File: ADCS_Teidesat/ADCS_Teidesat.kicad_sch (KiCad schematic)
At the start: 27 parts, among them U1 MAX2659ELT+T, U2 L86-M33, U3 LSM6DSV16XTR, U4 LIS2MDLTR, U5 TMS5703137DPGEQQ1, Y1 ATX-H13-F-16.000MHz-G100-T

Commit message: Mejora del enrutado y las conexiones de los componentes, además de la  modificación en la distribución de los planos
Optimización de las conexiones, liberando la capa TOP relazándolas en la capa BOTTON. Modificación de la distribución de los planos. Actualmente: TOP Layer (Plano de conexiones 1), Inner Layer 1 (GND), Inner Layer 2 (3V3) y BOTTON Layer (Plano de conexiones 2)
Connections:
- net +3V3: now also H1.47 (Pin_47), H1.48 (Pin_48), H1.49 (Pin_49), H1.50 (Pin_50), H1.51 (Pin_51), H1.52 (Pin_52), H2.18 (Pin_18), H2.19 (Pin_19), H2.20 (Pin_20)
- no-connect marks 238 -> 229
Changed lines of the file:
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@@
 	)
 	(no_connect
-		(at 355.6 102.87)
-	)
-	(no_connect
 		(at 234.95 185.42)
 	)
@@
 	)
 	(no_connect
-		(at 391.16 64.77)
-	)
-	(no_connect
 		(at 391.16 49.53)
 	)
@@
 	)
 	(no_connect
-		(at 391.16 67.31)
-	)
-	(no_connect
 		(at 355.6 59.69)
 	)
@@
 	)
 	(no_connect
-		(at 342.9 105.41)
-	)
-	(no_connect
 		(at 179.07 114.3)
 	)
@@
 	)
 	(no_connect
-		(at 355.6 105.41)
-	)
-	(no_connect
 		(at 342.9 74.93)
 	)
@@
 	)
 	(no_connect
-		(at 355.6 107.95)
-	)
-	(no_connect
 		(at 283.21 124.46)
 	)
@@
 	)
 	(no_connect
-		(at 342.9 107.95)
-	)
-	(no_connect
 		(at 342.9 49.53)
 	)
@@
 	)
 	(no_connect
-		(at 378.46 67.31)
-	)
-	(no_connect
 		(at 342.9 72.39)
 	)
@@
 	)
 	(no_connect
-		(at 342.9 102.87)
-	)
-	(no_connect
 		(at 189.23 30.48)
 	)
@@
 	(wire
 		(pts
+			(xy 364.49 102.87) (xy 355.6 102.87)
+		)
+		(stroke
+			(width 0)
+			(type default)
+		)
+	)
+	(wire
+		(pts
 			(xy 91.44 156.21) (xy 95.25 156.21)
 		)
@@
 	(wire
 		(pts
+			(xy 334.01 107.95) (xy 342.9 107.95)
+		)
+		(stroke
+			(width 0)
+			(type default)
+		)
+	)
+	(wire
+		(pts
 			(xy 88.9 229.87) (xy 95.25 229.87)
 		)
@@
 	(wire
 		(pts
+			(xy 400.05 64.77) (xy 391.16 64.77)
+		)
+		(stroke
+			(width 0)
+			(type default)
+		)
+	)
+	(wire
+		(pts
 			(xy 85.09 147.32) (xy 95.25 147.32)
 		)
@@
 	(wire
 		(pts
+			(xy 364.49 105.41) (xy 355.6 105.41)
+		)
+		(stroke
+			(width 0)
+			(type default)
+		)
+	)
+	(wire
+		(pts
 			(xy 43.18 227.33) (xy 25.4 227.33)
 		)
@@
 	(wire
 		(pts
+			(xy 369.57 67.31) (xy 378.46 67.31)
+		)
+		(stroke
+			(width 0)
+			(type default)
+		)
+	)
+	(wire
+		(pts
 			(xy 24.13 95.25) (xy 22.86 95.25)
 		)
@@
 	(wire
 		(pts
+			(xy 400.05 67.31) (xy 391.16 67.31)
+		)
+		(stroke
+			(width 0)
+			(type default)
+		)
+	)
+	(wire
+		(pts
 			(xy 50.8 264.16) (xy 50.8 266.7)
 		)
@@
 	(wire
 		(pts
+			(xy 364.49 107.95) (xy 355.6 107.95)
+		)
+		(stroke
+			(width 0)
+			(type default)
+		)
+	)
+	(wire
+		(pts
 			(xy 217.17 224.79) (xy 217.17 237.49)
 		)
@@
 	(wire
 		(pts
+			(xy 334.01 102.87) (xy 342.9 102.87)
+		)
+		(stroke
+			(width 0)
+			(type default)
+		)
+	)
+	(wire
+		(pts
 			(xy 102.87 218.44) (xy 102.87 227.33)
 		)
@@
 	(wire
 		(pts
+			(xy 334.01 105.41) (xy 342.9 105.41)
+		)
+		(stroke
+			(width 0)
+			(type default)
+		)
+	)
+	(wire
+		(pts
 			(xy 205.74 234.95) (xy 205.74 251.46)
 		)
@@
 		)
 	)
+	(label "+3V3"
+		(at 364.49 105.41 180)
+		(effects
+			(font
+				(size 1.27 1.27)
+			)
+			(justify right bottom)
+		)
+	)
 	(label "SPC_MAG."
 		(at 304.8 91.44 180)
@@
 		)
 	)
+	(label "+3V3"
+		(at 400.05 67.31 180)
+		(effects
+			(font
+				(size 1.27 1.27)
+			)
+			(justify right bottom)
+		)
+	)
 	(label "SOMI_IMU"
 		(at 304.8 83.82 180)
@@
 		)
 	)
+	(label "+3V3"
+		(at 334.01 105.41 0)
+		(effects
+			(font
+				(size 1.27 1.27)
+			)
+			(justify left bottom)
+		)
+	)
 	(label "DATA_OUT"
 		(at 78.74 154.94 180)
@@
 		)
 	)
+	(label "+3V3"
+		(at 369.57 67.31 0)
+		(effects
+			(font
+				(size 1.27 1.27)
+			)
+			(justify left bottom)
+		)
+	)
 	(label "CS_MAGNETÓMETRO"
 		(at 157.48 111.76 0)
@@
 		)
 	)
+	(label "+3V3"
+		(at 364.49 102.87 180)
+		(effects
+			(font
+				(size 1.27 1.27)
+			)
+			(justify right bottom)
+		)
+	)
 	(label "INT_MAGNETÓMETRO"
 		(at 215.9 232.41 180)
@@
 		)
 	)
+	(label "+3V3"
+		(at 334.01 102.87 0)
+		(effects
+			(font
+				(size 1.27 1.27)
+			)
+			(justify left bottom)
+		)
+	)
 	(label "INT1"
 		(at 34.29 232.41 0)
@@
 		)
 	)
+	(label "+3V3"
+		(at 400.05 64.77 180)
+		(effects
+			(font
+				(size 1.27 1.27)
+			)
+			(justify right bottom)
+		)
+	)
 	(label "INT1"
 		(at 168.91 78.74 0)
@@
 		)
 	)
+	(label "+3V3"
+		(at 364.49 107.95 180)
+		(effects
+			(font
+				(size 1.27 1.27)
+			)
+			(justify right bottom)
+		)
+	)
 	(label "OUT_ANT"
 		(at 60.96 165.1 180)
@@
 		)
 	)
+	(label "+3V3"
+		(at 334.01 107.95 0)
+		(effects
+			(font
+				(size 1.27 1.27)
+			)
+			(justify left bottom)
+		)
+	)
 	(label "RF"
 		(at 58.42 92.71 180)
@@
 		)
 		(property "Value" "+3V3"
-			(at 214.122 220.98 0)
+			(at 213.868 220.726 0)
 			(effects
 				(font

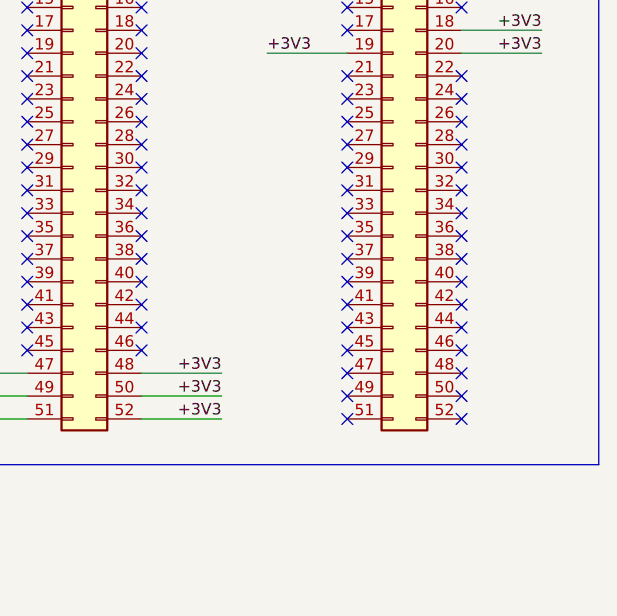
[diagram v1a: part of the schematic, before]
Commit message: Últimas modificaciones de la V.0.1.
Se han realizado las últimas modificaciones en del diseño de la PCB, se han nombrado las capas, y además, se han añadido las huellas correctas de cada componente.
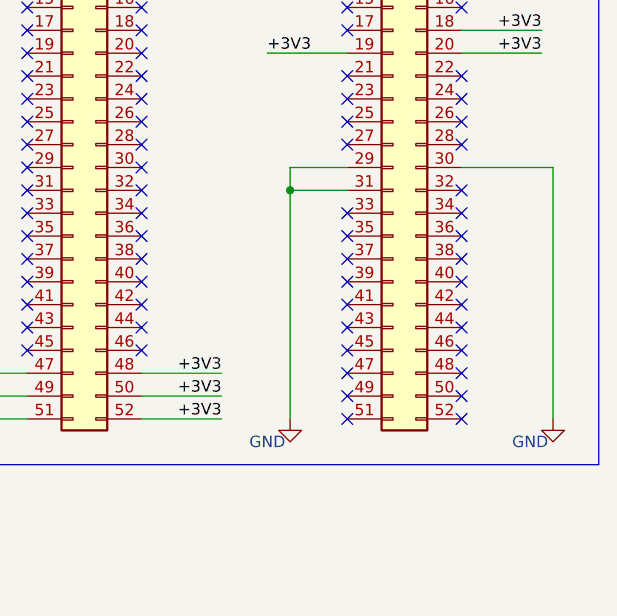
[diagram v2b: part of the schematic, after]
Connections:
- net GND: now also H2.29 (Pin_29), H2.30 (Pin_30), H2.31 (Pin_31)
- no-connect marks 229 -> 226
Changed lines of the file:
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@@
 	)
 	(junction
+		(at 372.11 82.55)
+		(diameter 0)
+		(color 0 0 0 0)
+	)
+	(junction
 		(at 64.77 116.84)
 		(diameter 0)
@@
 	)
 	(no_connect
-		(at 378.46 82.55)
-	)
-	(no_connect
 		(at 234.95 185.42)
 	)
@@
 	)
 	(no_connect
-		(at 391.16 80.01)
-	)
-	(no_connect
 		(at 342.9 44.45)
 	)
@@
 	)
 	(no_connect
-		(at 378.46 80.01)
-	)
-	(no_connect
 		(at 378.46 57.15)
 	)
@@
 	(wire
 		(pts
+			(xy 372.11 82.55) (xy 378.46 82.55)
+		)
+		(stroke
+			(width 0)
+			(type default)
+		)
+	)
+	(wire
+		(pts
 			(xy 66.04 250.19) (xy 66.04 266.7)
 		)
@@
 	(wire
 		(pts
+			(xy 401.32 80.01) (xy 401.32 107.95)
+		)
+		(stroke
+			(width 0)
+			(type default)
+		)
+	)
+	(wire
+		(pts
 			(xy 25.4 72.39) (xy 25.4 73.66)
 		)
@@
 	(wire
 		(pts
+			(xy 391.16 80.01) (xy 401.32 80.01)
+		)
+		(stroke
+			(width 0)
+			(type default)
+		)
+	)
+	(wire
+		(pts
 			(xy 54.61 92.71) (xy 58.42 92.71)
 		)
@@
 	(wire
 		(pts
+			(xy 372.11 107.95) (xy 372.11 82.55)
+		)
+		(stroke
+			(width 0)
+			(type default)
+		)
+	)
+	(wire
+		(pts
 			(xy 369.57 67.31) (xy 378.46 67.31)
 		)
@@
 	(wire
 		(pts
+			(xy 372.11 80.01) (xy 378.46 80.01)
+		)
+		(stroke
+			(width 0)
+			(type default)
+		)
+	)
+	(wire
+		(pts
 			(xy 205.74 251.46) (xy 217.17 251.46)
 		)
@@
 	(wire
 		(pts
+			(xy 372.11 82.55) (xy 372.11 80.01)
+		)
+		(stroke
+			(width 0)
+			(type default)
+		)
+	)
+	(wire
+		(pts
 			(xy 26.67 72.39) (xy 25.4 72.39)
 		)
@@
 	)
 	(symbol
+		(lib_id "power:GND")
+		(at 372.11 107.95 0)
+		(unit 1)
+		(exclude_from_sim no)
+		(in_bom yes)
+		(on_board yes)
+		(dnp no)
+		(property "Reference" "#PWR026"
+			(at 372.11 114.3 0)
+			(effects
+				(font
+					(size 1.27 1.27)
+				)
+				(hide yes)
+			)
+		)
+		(property "Value" "GND"
+			(at 369.57 110.49 0)
+			(effects
+				(font
+					(size 1.27 1.27)
+				)
+			)
+		)
+		(property "Footprint" ""
+			(at 372.11 107.95 0)
+			(effects
+				(font
+					(size 1.27 1.27)
+				)
+				(hide yes)
+			)
+		)
+		(property "Datasheet" ""
+			(at 372.11 107.95 0)
+			(effects
+				(font
+					(size 1.27 1.27)
+				)
+				(hide yes)
+			)
+		)
+		(property "Description" ""
+			(at 372.11 107.95 0)
+			(effects
+				(font
+					(size 1.27 1.27)
+				)
+			)
+		)
+		(pin "1"
+		)
+		(instances
+			(project "ADCS_Teidesat"
+				(path "/983c426c-24e0-4c65-ab69-1f1824adc5c6"
+					(reference "#PWR026")
+					(unit 1)
+				)
+			)
+		)
+	)
+	(symbol
 		(lib_id "power:+3V3")
 		(at 20.32 215.9 0)
@@
 					(unit 1)
 				)
+			)
+		)
+	)
+	(symbol
+		(lib_id "power:GND")
+		(at 401.32 107.95 0)
+		(unit 1)
+		(exclude_from_sim no)
+		(in_bom yes)
+		(on_board yes)
+		(dnp no)
+		(property "Reference" "#PWR027"
+			(at 401.32 114.3 0)
+			(effects
+				(font
+					(size 1.27 1.27)
+				)
+				(hide yes)
+			)
+		)
+		(property "Value" "GND"
+			(at 398.78 110.49 0)
+			(effects
+				(font
+					(size 1.27 1.27)
+				)
+			)
+		)
+		(property "Footprint" ""
+			(at 401.32 107.95 0)
+			(effects
+				(font
+					(size 1.27 1.27)
+				)
+				(hide yes)
+			)
+		)
+		(property "Datasheet" ""
+			(at 401.32 107.95 0)
+			(effects
+				(font
+					(size 1.27 1.27)
+				)
+				(hide yes)
+			)
+		)
+		(property "Description" ""
+			(at 401.32 107.95 0)
+			(effects
+				(font
+					(size 1.27 1.27)
+				)
+			)
+		)
+		(pin "1"
+		)
+		(instances
+			(project "ADCS_Teidesat"
+				(path "/983c426c-24e0-4c65-ab69-1f1824adc5c6"
+					(reference "#PWR027")
+					(unit 1)
+				)

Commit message: Modificación en la huella del módulo GNSS
He añadido un pin que añadimos en el esquemático al símbolo del modulo GNSS, el pin 13. Hemos añadido dicho pin a la huella del componente.

Co-Authored-By: hugohdezmo <238262256+hugohdezmo@users.noreply.github.com>
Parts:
- U2: footprint Huellas ADCS:L80-M39 -> Huellas ADCS:Prueba_MODULOGNSS
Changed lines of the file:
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@@
 			)
 		)
-		(property "Footprint" "Huellas ADCS:L80-M39"
+		(property "Footprint" "Huellas ADCS:Prueba_MODULOGNSS"
 			(at 66.04 239.7 0)
 			(effects
